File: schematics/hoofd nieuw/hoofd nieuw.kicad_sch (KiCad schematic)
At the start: 39 parts, among them J1 Conn_01x04_Pin, J2 Conn_01x02_Pin, J3 SFR02, J4 Conn_01x03_Pin, U1 ATtiny402-SS, U2 BH1750FVI-TR, U3 BH1750FVI-TR, Y1 ECS-2333MV-100-BN-TR

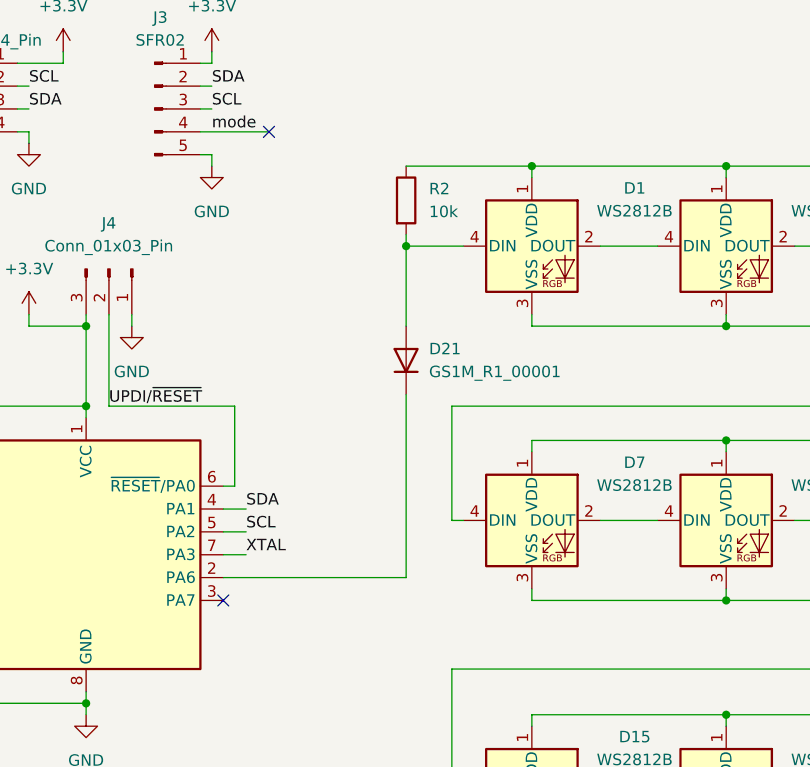
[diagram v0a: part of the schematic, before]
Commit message: led van het 'mondje' zijn geplaatst
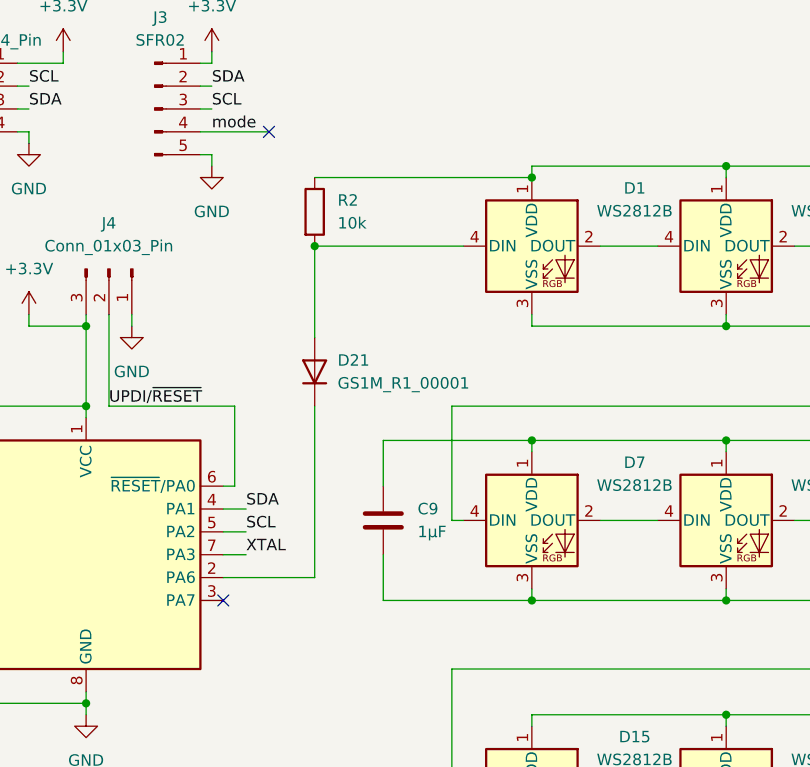
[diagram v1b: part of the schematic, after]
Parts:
- added C9: 1µF, Capacitor_SMD:C_0603_1608Metric, symbol Device:C
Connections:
- net +5V: now also C9.1
- net GND: now also C9.2
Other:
- moved on the sheet: D21, R2
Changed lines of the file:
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@@
 	)
 	(junction
-		(at 92.71 45.72)
-		(diameter 0)
-		(color 0 0 0 0)
-	)
-	(junction
 		(at 128.27 54.61)
 		(diameter 0)
@@
 	)
 	(junction
+		(at 106.68 85.09)
+		(diameter 0)
+		(color 0 0 0 0)
+	)
+	(junction
 		(at 128.27 67.31)
 		(diameter 0)
@@
 	)
 	(junction
+		(at 82.55 45.72)
+		(diameter 0)
+		(color 0 0 0 0)
+	)
+	(junction
 		(at 134.62 153.67)
 		(diameter 0)
@@
 	)
 	(junction
+		(at 106.68 38.1)
+		(diameter 0)
+		(color 0 0 0 0)
+	)
+	(junction
 		(at 127 149.86)
 		(diameter 0)
@@
 	)
 	(junction
+		(at 106.68 67.31)
+		(diameter 0)
+		(color 255 0 0 1)
+	)
+	(junction
 		(at 171.45 67.31)
 		(diameter 0)
@@
 	)
 	(junction
-		(at 106.68 36.83)
-		(diameter 0)
-		(color 255 0 0 1)
-	)
-	(junction
 		(at 214.63 67.31)
 		(diameter 0)
@@
 	(wire
 		(pts
-			(xy 106.68 36.83) (xy 106.68 38.1)
-		)
-		(stroke
-			(width 0)
-			(type default)
-			(color 255 0 0 1)
-		)
-	)
-	(wire
-		(pts
 			(xy 49.53 33.02) (xy 50.8 33.02)
 		)
@@
 	(wire
 		(pts
-			(xy 92.71 62.23) (xy 92.71 82.55)
+			(xy 82.55 63.5) (xy 82.55 82.55)
 		)
 		(stroke
@@
 	(wire
 		(pts
-			(xy 92.71 54.61) (xy 92.71 45.72)
+			(xy 82.55 55.88) (xy 82.55 45.72)
 		)
 		(stroke
@@
 	(wire
 		(pts
+			(xy 106.68 67.31) (xy 90.17 67.31)
+		)
+		(stroke
+			(width 0)
+			(type default)
+			(color 255 0 0 1)
+		)
+	)
+	(wire
+		(pts
 			(xy 171.45 36.83) (xy 149.86 36.83)
 		)
@@
 	(wire
 		(pts
+			(xy 82.55 45.72) (xy 99.06 45.72)
+		)
+		(stroke
+			(width 0)
+			(type default)
+		)
+	)
+	(wire
+		(pts
 			(xy 128.27 97.79) (xy 128.27 99.06)
 		)
@@
 	(wire
 		(pts
+			(xy 90.17 67.31) (xy 90.17 72.39)
+		)
+		(stroke
+			(width 0)
+			(type default)
+			(color 255 0 0 1)
+		)
+	)
+	(wire
+		(pts
 			(xy 149.86 85.09) (xy 171.45 85.09)
 		)
@@
 	(wire
 		(pts
-			(xy 72.39 82.55) (xy 92.71 82.55)
+			(xy 72.39 82.55) (xy 82.55 82.55)
 		)
 		(stroke
@@
 	(wire
 		(pts
-			(xy 106.68 36.83) (xy 92.71 36.83)
+			(xy 106.68 38.1) (xy 82.55 38.1)
 		)
 		(stroke
@@
 	(wire
 		(pts
-			(xy 92.71 45.72) (xy 99.06 45.72)
+			(xy 106.68 99.06) (xy 106.68 97.79)
 		)
 		(stroke
 			(width 0)
 			(type default)
+			(color 255 0 0 1)
 		)
 	)
 	(wire
 		(pts
-			(xy 106.68 99.06) (xy 106.68 97.79)
+			(xy 149.86 83.82) (xy 149.86 85.09)
 		)
 		(stroke
 			(width 0)
 			(type default)
-			(color 255 0 0 1)
 		)
 	)
 	(wire
 		(pts
-			(xy 149.86 83.82) (xy 149.86 85.09)
+			(xy 99.06 76.2) (xy 97.79 76.2)
 		)
 		(stroke
@@
 	(wire
 		(pts
-			(xy 99.06 76.2) (xy 97.79 76.2)
+			(xy 90.17 80.01) (xy 90.17 85.09)
 		)
 		(stroke
@@
 	(wire
 		(pts
+			(xy 106.68 38.1) (xy 106.68 36.83)
+		)
+		(stroke
+			(width 0)
+			(type default)
+			(color 255 0 0 1)
+		)
+	)
+	(wire
+		(pts
 			(xy 57.15 96.52) (xy 57.15 97.79)
 		)
@@
 	(wire
 		(pts
-			(xy 92.71 44.45) (xy 92.71 45.72)
-		)
-		(stroke
-			(width 0)
-			(type default)
-		)
-	)
-	(wire
-		(pts
 			(xy 67.31 115.57) (xy 69.85 115.57)
 		)
@@
 	(wire
 		(pts
+			(xy 90.17 85.09) (xy 106.68 85.09)
+		)
+		(stroke
+			(width 0)
+			(type default)
+		)
+	)
+	(wire
+		(pts
 			(xy 35.56 27.94) (xy 35.56 29.21)
 		)
@@
 	)
 	(symbol
+		(lib_id "Device:C")
+		(at 90.17 76.2 0)
+		(unit 1)
+		(exclude_from_sim no)
+		(in_bom yes)
+		(on_board yes)
+		(dnp no)
+		(fields_autoplaced yes)
+		(property "Reference" "C9"
+			(at 93.98 74.9299 0)
+			(effects
+				(font
+					(size 1.27 1.27)
+				)
+				(justify left)
+			)
+		)
+		(property "Value" "1µF"
+			(at 93.98 77.4699 0)
+			(effects
+				(font
+					(size 1.27 1.27)
+				)
+				(justify left)
+			)
+		)
+		(property "Footprint" "Capacitor_SMD:C_0603_1608Metric"
+			(at 91.1352 80.01 0)
+			(effects
+				(font
+					(size 1.27 1.27)
+				)
+				(hide yes)
+			)
+		)
+		(property "Datasheet" "~"
+			(at 90.17 76.2 0)
+			(effects
+				(font
+					(size 1.27 1.27)
+				)
+				(hide yes)
+			)
+		)
+		(property "Description" "Unpolarized capacitor"
+			(at 90.17 76.2 0)
+			(effects
+				(font
+					(size 1.27 1.27)
+				)
+				(hide yes)
+			)
+		)
+		(pin "1"
+		)
+		(pin "2"
+		)
+		(instances
+			(project "hoofd nieuw"
+				(path "/7e0a6d27-e85c-4a07-8035-4491285a0fea"
+					(reference "C9")
+					(unit 1)
+				)
+			)
+		)
+	)
+	(symbol
 		(lib_id "Device:D")
-		(at 92.71 58.42 90)
+		(at 82.55 59.69 90)
 		(unit 1)
 		(exclude_from_sim no)
@@
 		(fields_autoplaced yes)
 		(property "Reference" "D21"
-			(at 95.25 57.1499 90)
+			(at 85.09 58.4199 90)
 			(effects
 				(font
@@
 		)
 		(property "Value" "GS1M_R1_00001"
-			(at 95.25 59.6899 90)
+			(at 85.09 60.9599 90)
 			(effects
 				(font
@@
 		)
 		(property "Footprint" "Diode_SMD:D_SMA"
-			(at 92.71 58.42 0)
+			(at 82.55 59.69 0)
 			(effects
 				(font
@@
 		)
 		(property "Datasheet" "~"
-			(at 92.71 58.42 0)
+			(at 82.55 59.69 0)
 			(effects
 				(font
@@
 		)
 		(property "Description" "Diode"
-			(at 92.71 58.42 0)
+			(at 82.55 59.69 0)
 			(effects
 				(font
@@
 		)
 		(property "Sim.Device" "D"
-			(at 92.71 58.42 0)
+			(at 82.55 59.69 0)
 			(effects
 				(font
@@
 		)
 		(property "Sim.Pins" "1=K 2=A"
-			(at 92.71 58.42 0)
+			(at 82.55 59.69 0)
 			(effects
 				(font
@@
 	(symbol
 		(lib_id "Device:R")
-		(at 92.71 40.64 0)
+		(at 82.55 41.91 0)
 		(unit 1)
 		(exclude_from_sim no)
@@
 		(fields_autoplaced yes)
 		(property "Reference" "R2"
-			(at 95.25 39.3699 0)
+			(at 85.09 40.6399 0)
 			(effects
 				(font
@@
 		)
 		(property "Value" "10k"
-			(at 95.25 41.9099 0)
+			(at 85.09 43.1799 0)
 			(effects
 				(font
@@
 		)
 		(property "Footprint" "Resistor_SMD:R_0603_1608Metric"
-			(at 90.932 40.64 90)
+			(at 80.772 41.91 90)
 			(effects
 				(font
@@
 		)
 		(property "Datasheet" "~"
-			(at 92.71 40.64 0)
+			(at 82.55 41.91 0)
 			(effects
 				(font
@@
 		)
 		(property "Description" "Resistor"
-			(at 92.71 40.64 0)
+			(at 82.55 41.91 0)
 			(effects
 				(font

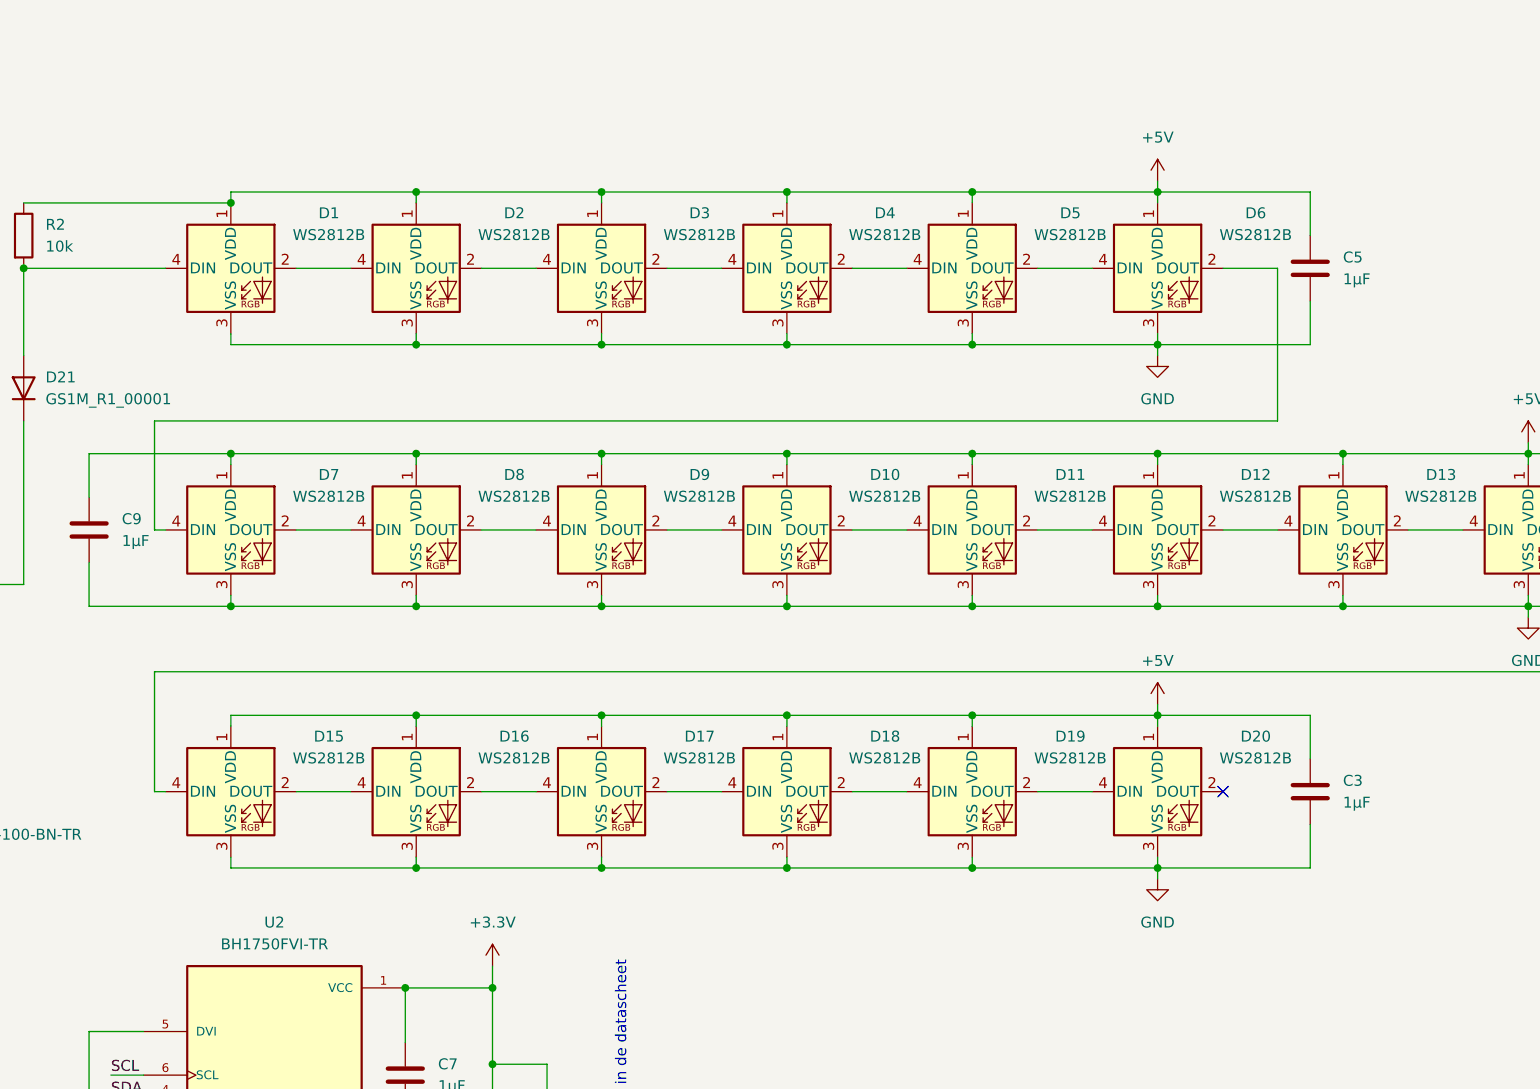
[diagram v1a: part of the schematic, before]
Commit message: de locatie van alle componenten is bepaald in het hoofd
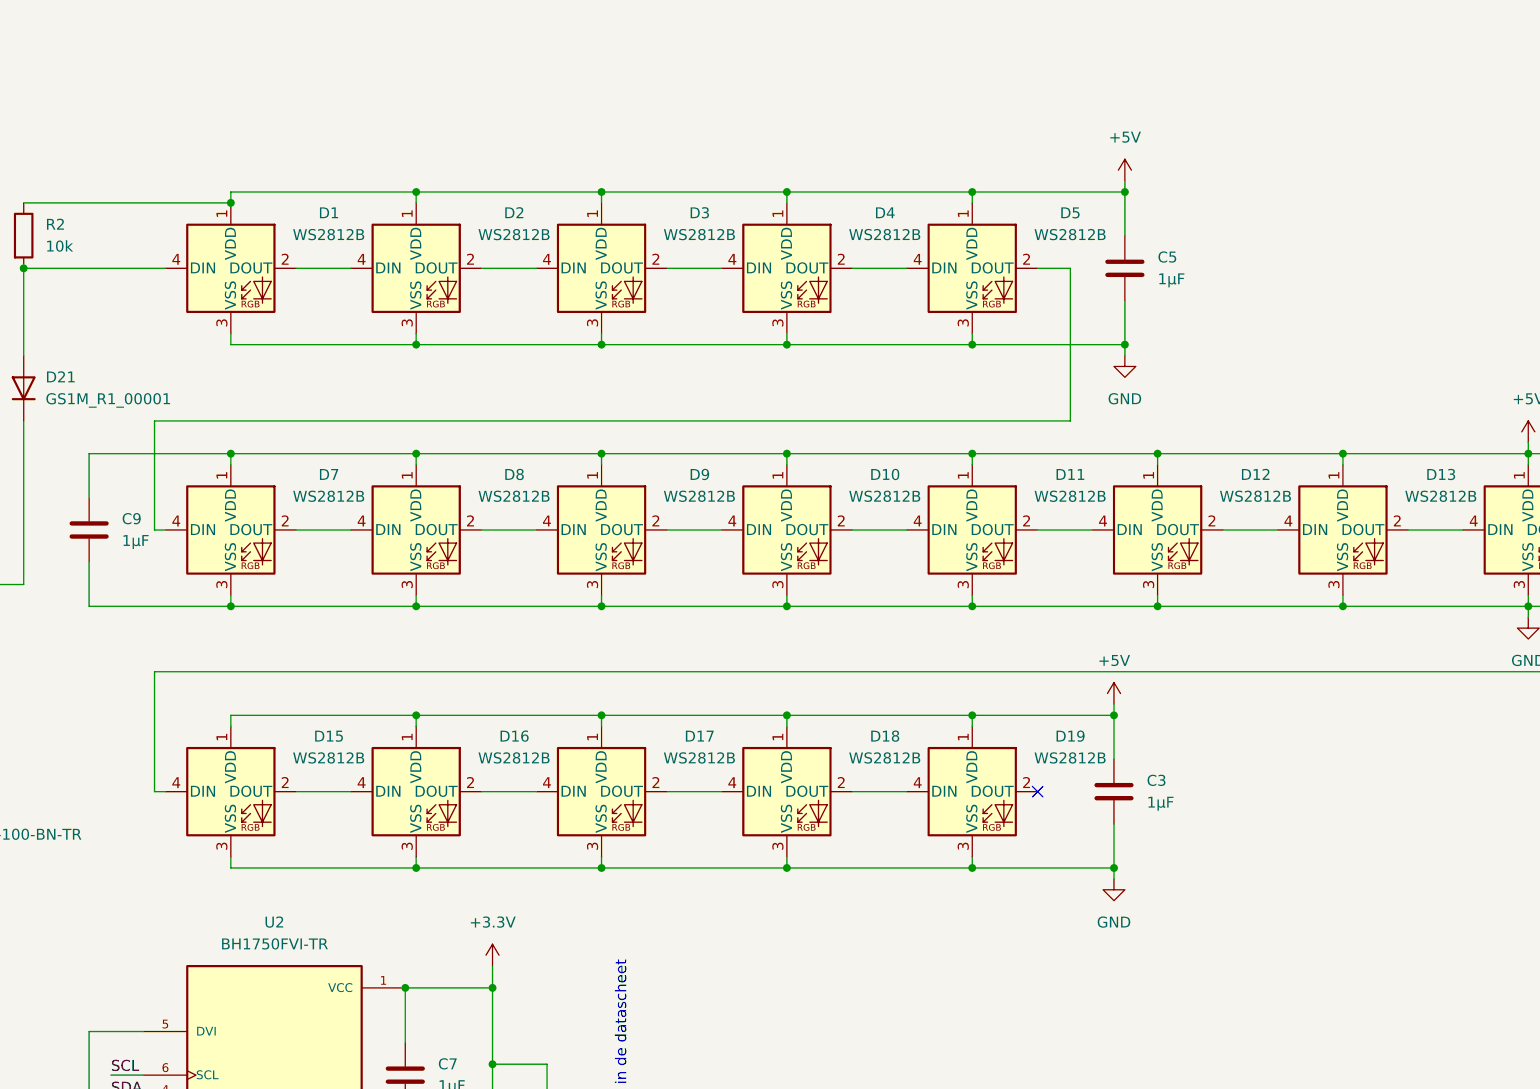
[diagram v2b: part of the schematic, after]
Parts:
- removed D20, D6: WS2812B, LED_SMD:LED_WS2812B_PLCC4_5.0x5.0mm_P3.2mm, symbol LED:WS2812B
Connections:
- net at D7.4 (DIN): now also D5.2 (DOUT)
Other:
- moved on the sheet: C3, C5

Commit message: maak de gbr file's voor nieuw hoofd
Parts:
- added D20: D5V0P4B5LP08, Library:D5V0P4B5LP08, symbol robot:D5V0P4B5LP08
- added D6: PESD5V0X1BCSFYL, PESD5V0X1BCSFYL:PMEG3005AESFYL, symbol PESD5V0X1BCSFYL:PESD5V0X1BCSFYL
- added R3: 5K1, Resistor_SMD:R_0603_1608Metric, symbol Device:R
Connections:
- net +3.3V: now also D20.1
- net +5V: now also D6.2 (K2)
- net GND: now also D20.GND, D6.1 (K1)
- net SCL: now also D20.2
- net SDA: now also D20.3
- net UPDI/~{RESET}: now also D20.4, R3.2; no longer J4.2 (Pin_2)
- new net: J4.2 (Pin_2), R3.1
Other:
- moved on the sheet: J1, J2, J3
